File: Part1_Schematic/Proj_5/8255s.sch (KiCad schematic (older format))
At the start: 18 parts, among them J1 Conn_02x15_Top_Bottom, J2 Conn_02x15_Top_Bottom, J3 Conn_02x15_Top_Bottom, U1 8255, U2 8255, U3 8255, U39 74LVC1G11, U40 74LVC1G11, U41 74AHC1G08, U42 74LVC1G11, U43 74AHC1G08, U44 74LVC1G11, U45 74AHC1G08, U46 74LVC1G11, U47 PAL16L8

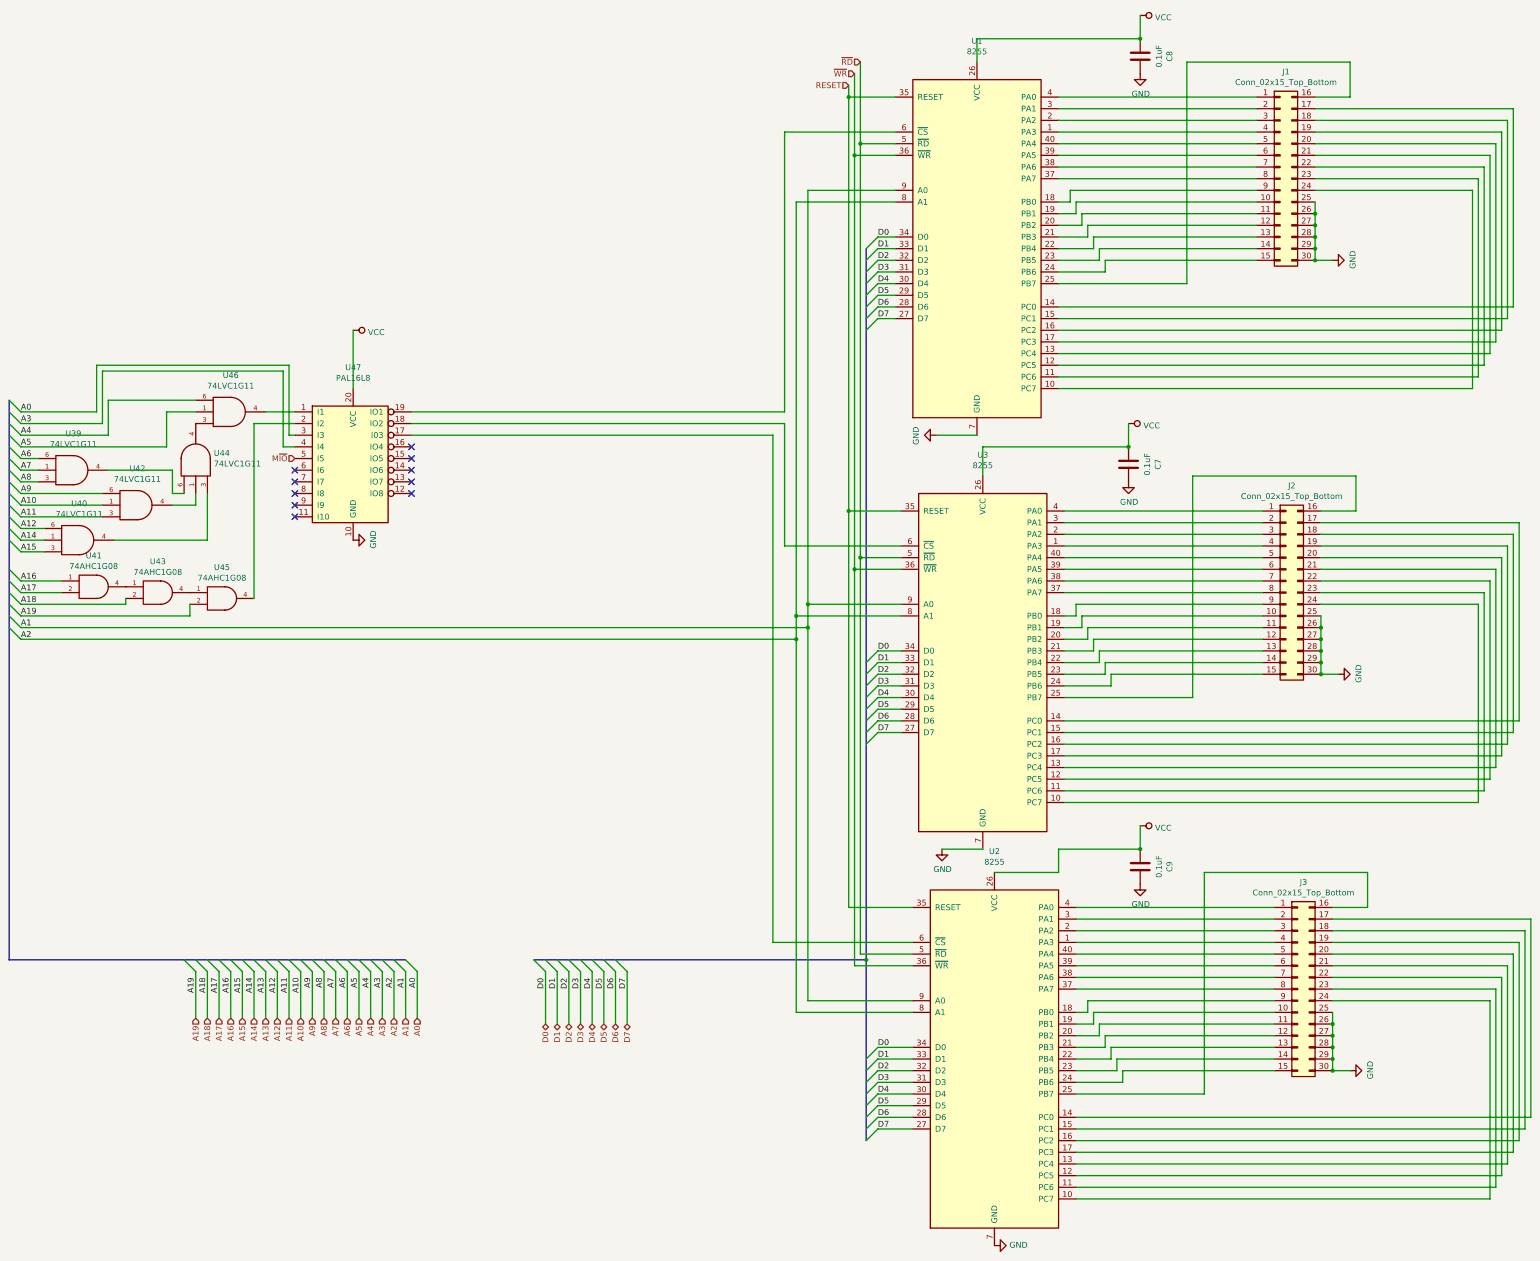
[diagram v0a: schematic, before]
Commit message: Addressing for 8279 and 8259
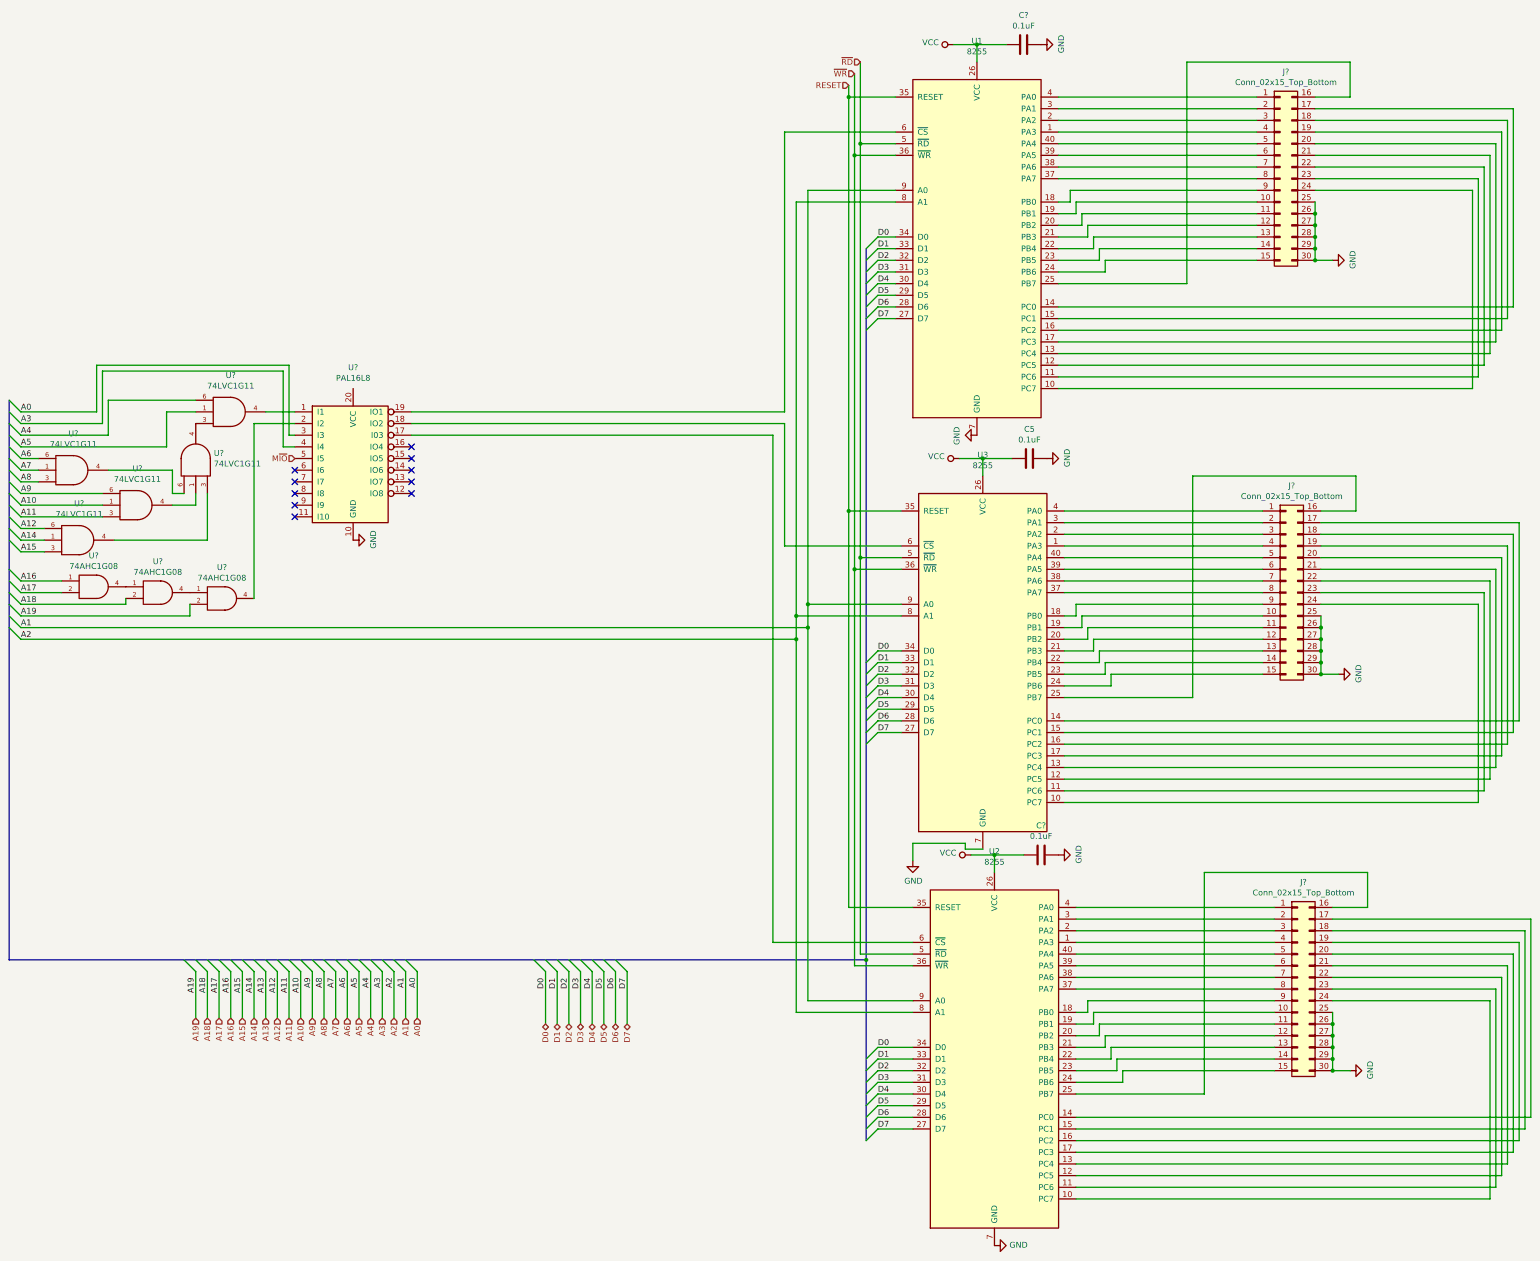
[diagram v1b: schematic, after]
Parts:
- removed C7, C8: 0.1uF, symbol Device:C
- added C5, C?: 0.1uF, symbol Device:C
- renumbered C9 to C?, J2 to J?, J1 to J?, J3 to J?, U47 to U?, U45 to U?, U43 to U?, U41 to U?, U40 to U?, U39 to U?, U42 to U?, U46 to U?, U44 to U?
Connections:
- net GND: now also C5.1, C?.1
- net VCC: now also C5.2, C?.2; no longer U?.20 (VCC)
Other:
- moved on the sheet: C?
